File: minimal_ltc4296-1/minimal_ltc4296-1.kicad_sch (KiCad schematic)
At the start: 44 parts, among them J1 TBP02R1-381-03BE, J2 TBP02R1-381-03BE, J3 TBP02R1-381-03BE, J4 TBP02R1-381-03BE, J5 TBP02R1-381-03BE, J6 TBP02R1-381-02BE, Q1 100.0 V, Q2 100.0 V, Q3 100.0 V, Q4 100.0 V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

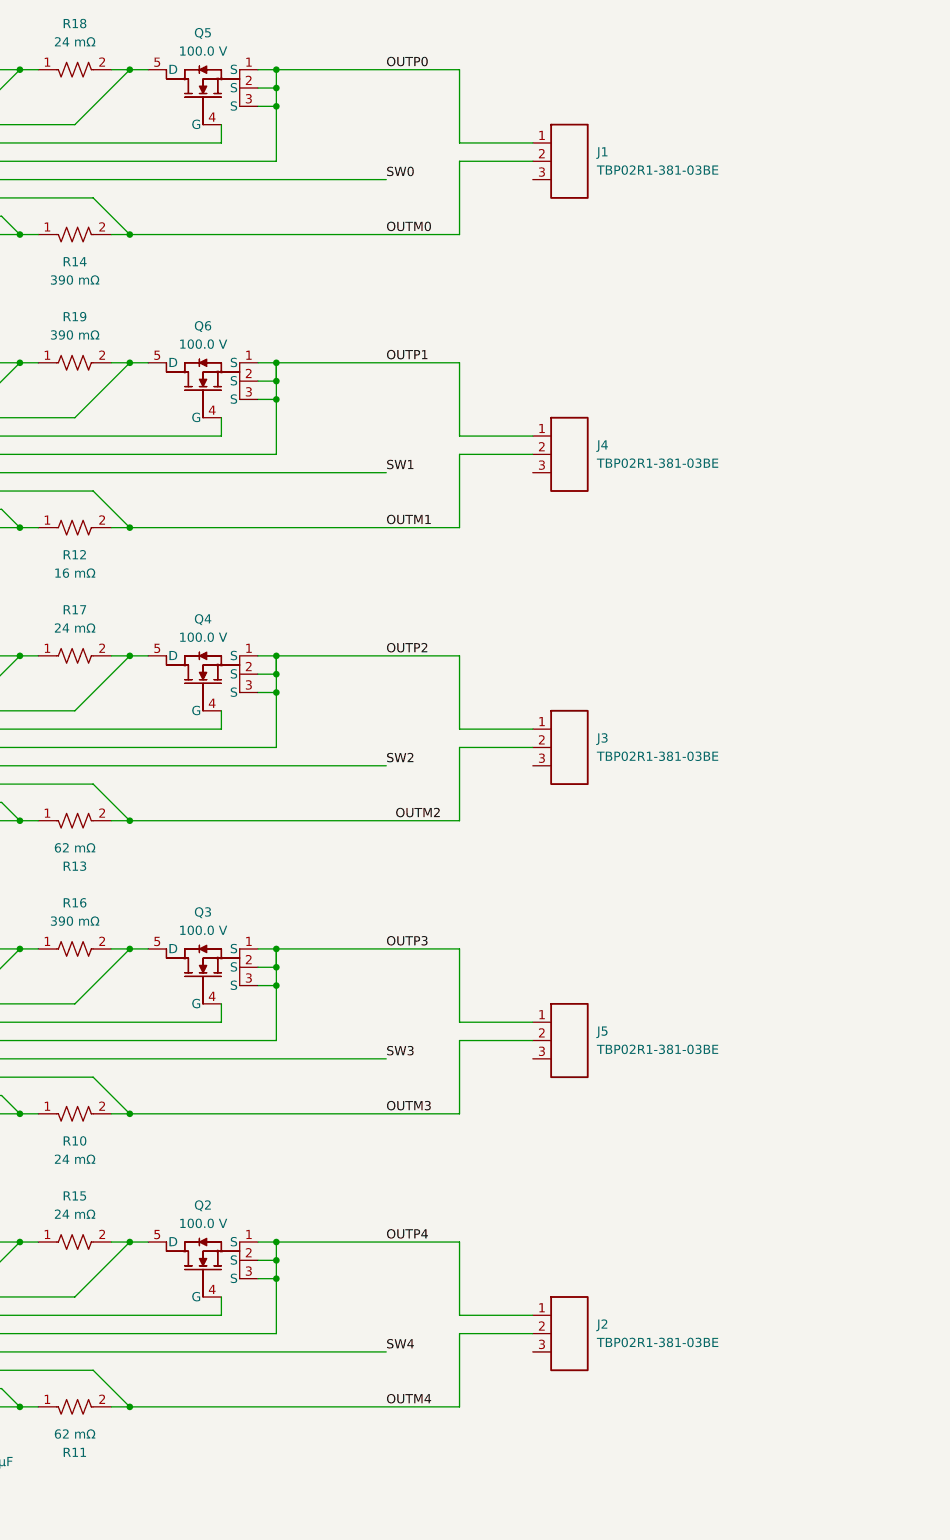
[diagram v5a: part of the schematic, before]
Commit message: Update KiCad project files and add SCCP Circuit 0 schematic
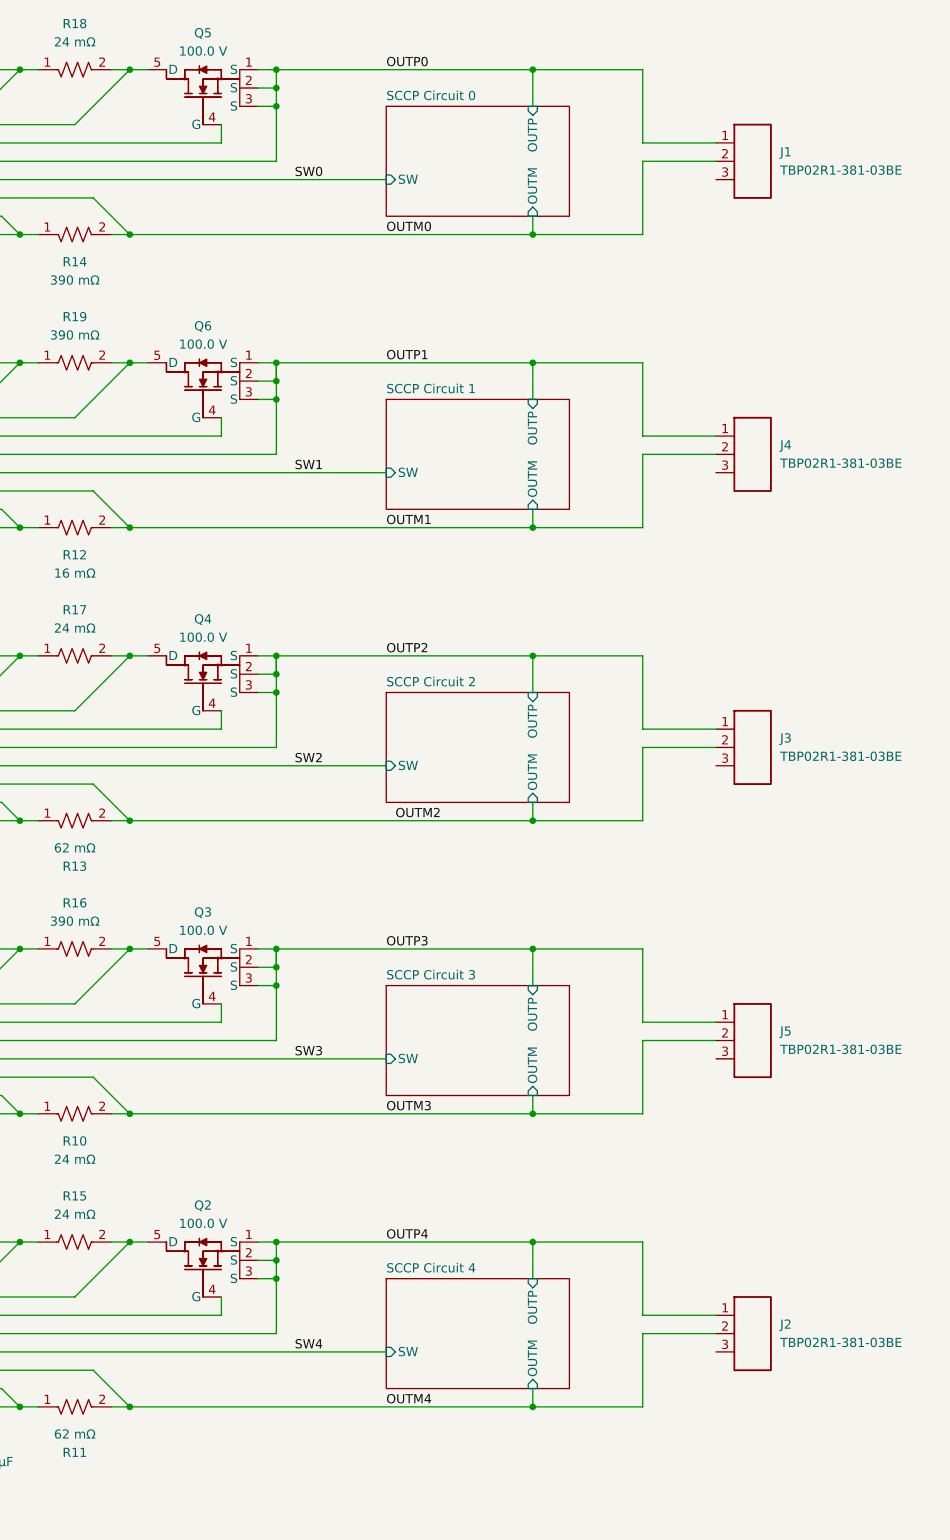
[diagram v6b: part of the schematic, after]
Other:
- added sheet SCCP Circuit 0 (SCCP Circuit 0.kicad_sch)
- added sheet SCCP Circuit 1 (SCCP Circuit 0.kicad_sch)
- added sheet SCCP Circuit 2 (SCCP Circuit 0.kicad_sch)
- added sheet SCCP Circuit 3 (SCCP Circuit 0.kicad_sch)
- added sheet SCCP Circuit 4 (SCCP Circuit 0.kicad_sch)
- moved on the sheet: J1, J2, J3, J4, J5

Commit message: Update KiCad PCB file
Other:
- sheet SCCP Circuit 0 ports: added 3V3; removed none
- sheet SCCP Circuit 1 ports: added 3V3; removed none
- sheet SCCP Circuit 2 ports: added 3V3; removed none
- sheet SCCP Circuit 3 ports: added 3V3; removed none
- sheet SCCP Circuit 4 ports: added 3V3; removed none
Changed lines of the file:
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@@
+			)
+		)
+		(pin "3V3" input
+			(at 330.2 127 180)
+			(effects
+				(font
+					(size 1.27 1.27)
+				)
+				(justify left)
 			)
 		)
@@
 			)
 		)
+		(pin "3V3" input
+			(at 330.2 45.72 180)
+			(effects
+				(font
+					(size 1.27 1.27)
+				)
+				(justify left)
+			)
+		)
 		(instances
 			(project "minimal_ltc4296-1"
@@
 			)
 		)
+		(pin "3V3" input
+			(at 330.2 167.64 180)
+			(effects
+				(font
+					(size 1.27 1.27)
+				)
+				(justify left)
+			)
+		)
 		(instances
 			(project "minimal_ltc4296-1"
@@
 			)
 		)
+		(pin "3V3" input
+			(at 330.2 208.28 180)
+			(effects
+				(font
+					(size 1.27 1.27)
+				)
+				(justify left)
+			)
+		)
 		(instances
 			(project "minimal_ltc4296-1"
@@
 			(effects
 				(font
+					(size 1.27 1.27)
+				)
+				(justify left)
+			)
+		)
+		(pin "3V3" input
+			(at 330.2 86.36 180)
+			(effects
+				(font

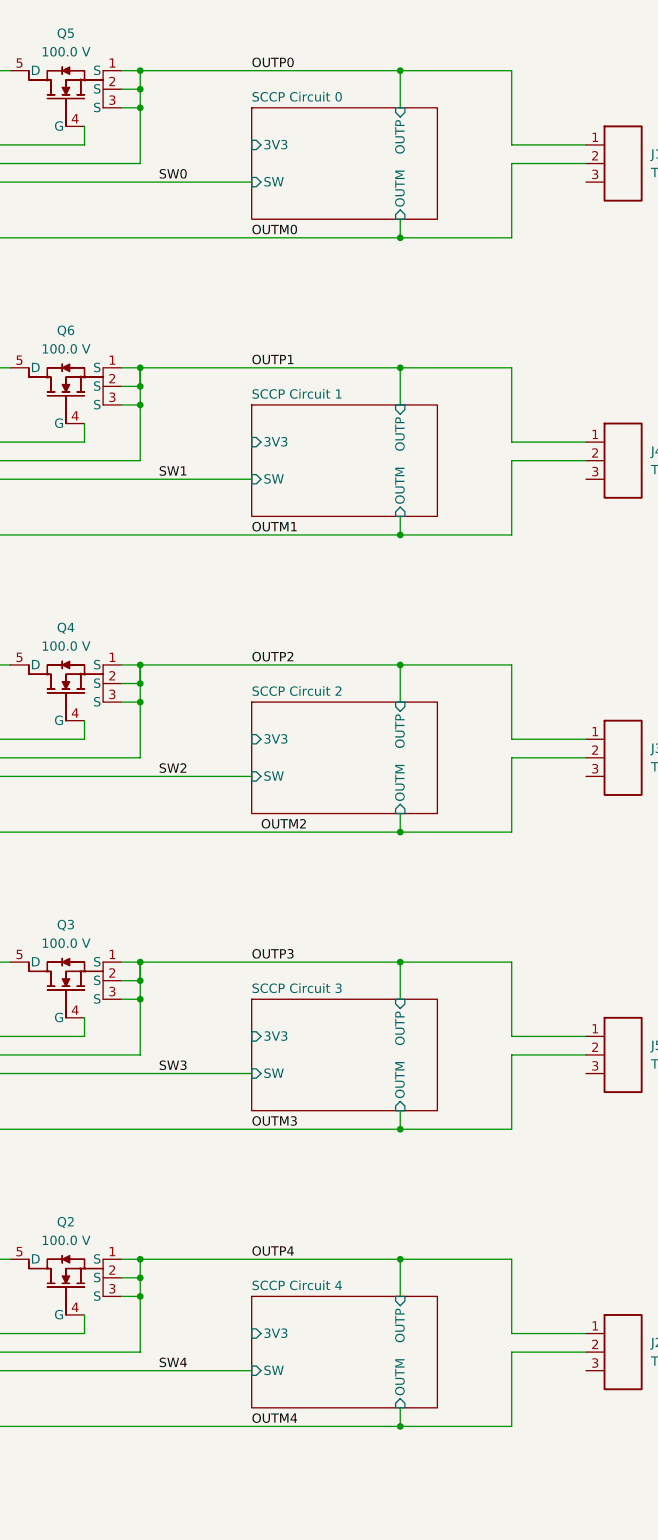
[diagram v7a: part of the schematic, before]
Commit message: Update KiCad schematic, PCB, and symbol libraries with SCCP circuit changes
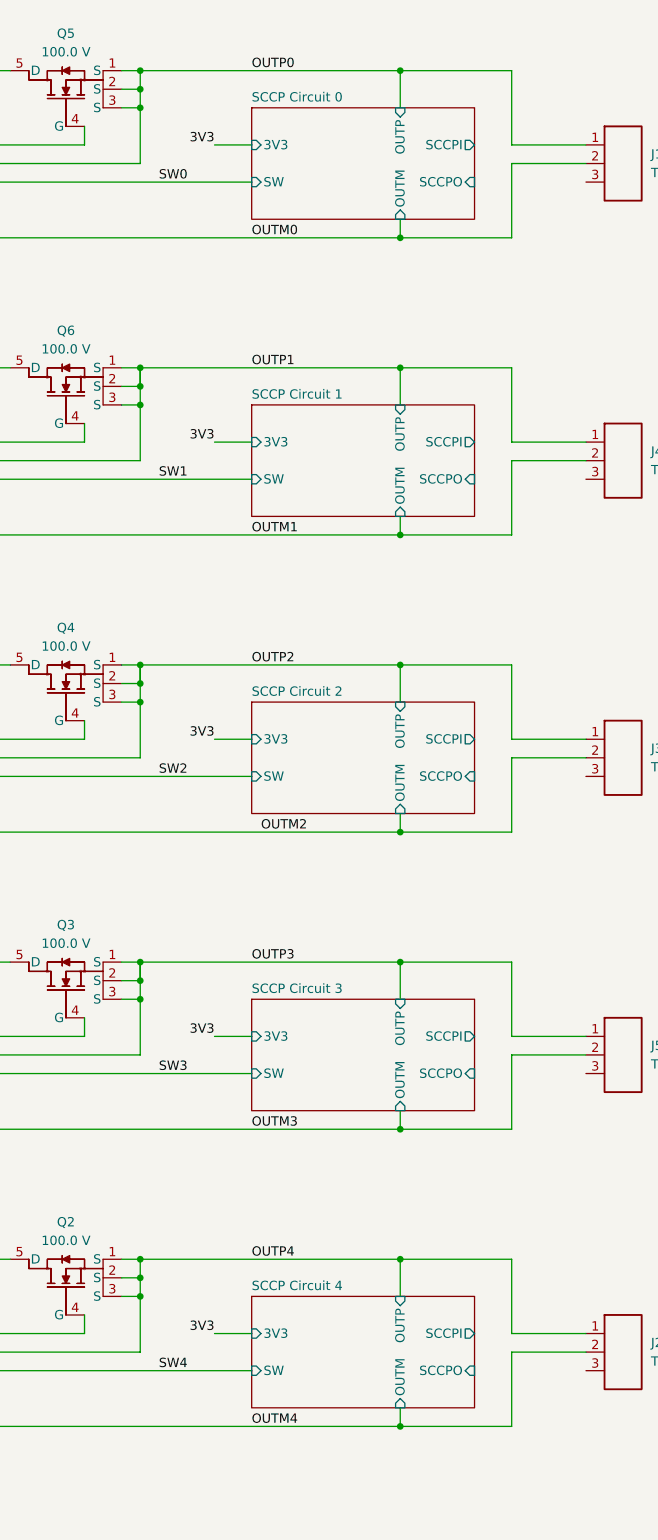
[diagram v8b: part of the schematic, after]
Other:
- sheet SCCP Circuit 0 ports: added SCCPI, SCCPO; removed none
- sheet SCCP Circuit 1 ports: added SCCPI, SCCPO; removed none
- sheet SCCP Circuit 2 ports: added SCCPI, SCCPO; removed none
- sheet SCCP Circuit 3 ports: added SCCPI, SCCPO; removed none
- sheet SCCP Circuit 4 ports: added SCCPI, SCCPO; removed none
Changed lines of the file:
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@@
 	(wire
 		(pts
+			(xy 325.12 127) (xy 330.2 127)
+		)
+		(stroke
+			(width 0)
+			(type default)
+		)
+	)
+	(wire
+		(pts
 			(xy 312.42 35.56) (xy 314.96 35.56)
 		)
@@
 	(wire
 		(pts
+			(xy 325.12 86.36) (xy 330.2 86.36)
+		)
+		(stroke
+			(width 0)
+			(type default)
+		)
+	)
+	(wire
+		(pts
 			(xy 177.8 62.23) (xy 177.8 63.5)
 		)
@@
 	(wire
 		(pts
+			(xy 325.12 167.64) (xy 330.2 167.64)
+		)
+		(stroke
+			(width 0)
+			(type default)
+		)
+	)
+	(wire
+		(pts
 			(xy 165.1 147.32) (xy 165.1 160.02)
 		)
@@
 	(wire
 		(pts
+			(xy 325.12 45.72) (xy 330.2 45.72)
+		)
+		(stroke
+			(width 0)
+			(type default)
+		)
+	)
+	(wire
+		(pts
 			(xy 220.98 93.98) (xy 289.56 93.98)
 		)
@@
 	(wire
 		(pts
+			(xy 325.12 208.28) (xy 330.2 208.28)
+		)
+		(stroke
+			(width 0)
+			(type default)
+		)
+	)
+	(wire
+		(pts
 			(xy 241.3 58.42) (xy 279.4 58.42)
 		)
@@
 		)
 	)
+	(label "3V3"
+		(at 325.12 208.28 180)
+		(effects
+			(font
+				(size 1.27 1.27)
+			)
+			(justify right bottom)
+		)
+	)
 	(label "SW2"
 		(at 317.5 132.08 0)
@@
 		)
 	)
+	(label "3V3"
+		(at 325.12 45.72 180)
+		(effects
+			(font
+				(size 1.27 1.27)
+			)
+			(justify right bottom)
+		)
+	)
 	(label "HGATE0"
 		(at 223.52 45.72 0)
@@
 		)
 	)
+	(label "3V3"
+		(at 325.12 167.64 180)
+		(effects
+			(font
+				(size 1.27 1.27)
+			)
+			(justify right bottom)
+		)
+	)
 	(label "LSNS"
 		(at 243.84 220.98 0)
@@
 		)
 	)
+	(label "3V3"
+		(at 325.12 86.36 180)
+		(effects
+			(font
+				(size 1.27 1.27)
+			)
+			(justify right bottom)
+		)
+	)
 	(label "PSE"
 		(at 116.84 30.48 0)
@@
 		)
 	)
+	(label "3V3"
+		(at 325.12 127 180)
+		(effects
+			(font
+				(size 1.27 1.27)
+			)
+			(justify right bottom)
+		)
+	)
 	(label "HSNSM1"
 		(at 223.52 83.82 0)
@@
 	(sheet
 		(at 330.2 121.92)
-		(size 25.4 15.24)
+		(size 30.48 15.24)
 		(exclude_from_sim no)
 		(in_bom yes)
@@
 			)
 		)
+		(pin "SCCPI" output
+			(at 360.68 127 0)
+			(effects
+				(font
+					(size 1.27 1.27)
+				)
+				(justify right)
+			)
+		)
+		(pin "SCCPO" input
+			(at 360.68 132.08 0)
+			(effects
+				(font
+					(size 1.27 1.27)
+				)
+				(justify right)
+			)
+		)
 		(instances
 			(project "minimal_ltc4296-1"
@@
 	(sheet
 		(at 330.2 40.64)
-		(size 25.4 15.24)
+		(size 30.48 15.24)
 		(exclude_from_sim no)
 		(in_bom yes)
@@
 			)
 		)
+		(pin "SCCPI" output
+			(at 360.68 45.72 0)
+			(effects
+				(font
+					(size 1.27 1.27)
+				)
+				(justify right)
+			)
+		)
+		(pin "SCCPO" input
+			(at 360.68 50.8 0)
+			(effects
+				(font
+					(size 1.27 1.27)
+				)
+				(justify right)
+			)
+		)
 		(instances
 			(project "minimal_ltc4296-1"
@@
 	(sheet
 		(at 330.2 162.56)
-		(size 25.4 15.24)
+		(size 30.48 15.24)
 		(exclude_from_sim no)
 		(in_bom yes)
@@
 			)
 		)
+		(pin "SCCPI" output
+			(at 360.68 167.64 0)
+			(effects
+				(font
+					(size 1.27 1.27)
+				)
+				(justify right)
+			)
+		)
+		(pin "SCCPO" input
+			(at 360.68 172.72 0)
+			(effects
+				(font
+					(size 1.27 1.27)
+				)
+				(justify right)
+			)
+		)
 		(instances
 			(project "minimal_ltc4296-1"
@@
 	(sheet
 		(at 330.2 203.2)
-		(size 25.4 15.24)
+		(size 30.48 15.24)
 		(exclude_from_sim no)
 		(in_bom yes)
@@
 			)
 		)
+		(pin "SCCPI" output
+			(at 360.68 208.28 0)
+			(effects
+				(font
+					(size 1.27 1.27)
+				)
+				(justify right)
+			)
+		)
+		(pin "SCCPO" input
+			(at 360.68 213.36 0)
+			(effects
+				(font
+					(size 1.27 1.27)
+				)
+				(justify right)
+			)
+		)
 		(instances
 			(project "minimal_ltc4296-1"
@@
 	(sheet
 		(at 330.2 81.28)
-		(size 25.4 15.24)
+		(size 30.48 15.24)
 		(exclude_from_sim no)
 		(in_bom yes)
@@
 			)
 		)
+		(pin "SCCPI" output
+			(at 360.68 86.36 0)
+			(effects
+				(font
+					(size 1.27 1.27)
+				)
+				(justify right)
+			)
+		)
+		(pin "SCCPO" input
+			(at 360.68 91.44 0)
+			(effects
+				(font
+					(size 1.27 1.27)
+				)
+				(justify right)
+			)
+		)
